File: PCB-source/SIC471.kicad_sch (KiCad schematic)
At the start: 15 parts, among them U9 SIC477ED-T1-GE3

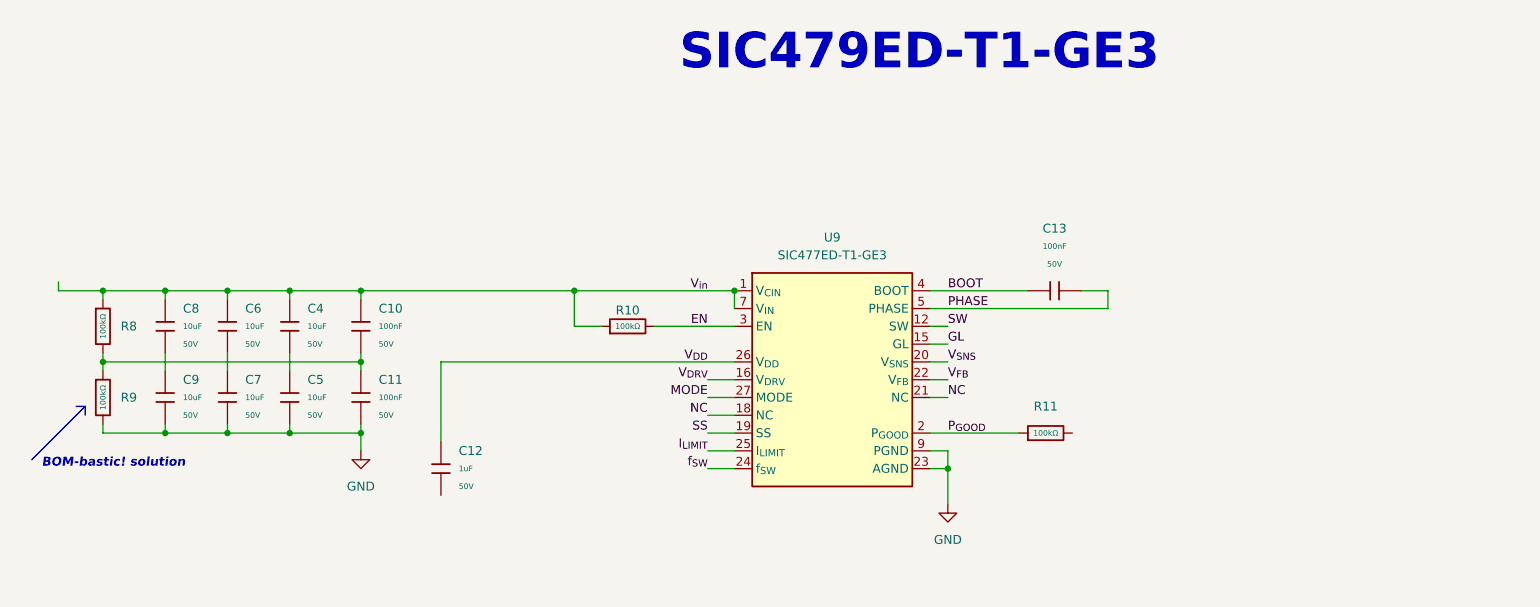
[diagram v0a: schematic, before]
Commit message: Finish component and diffpair placement
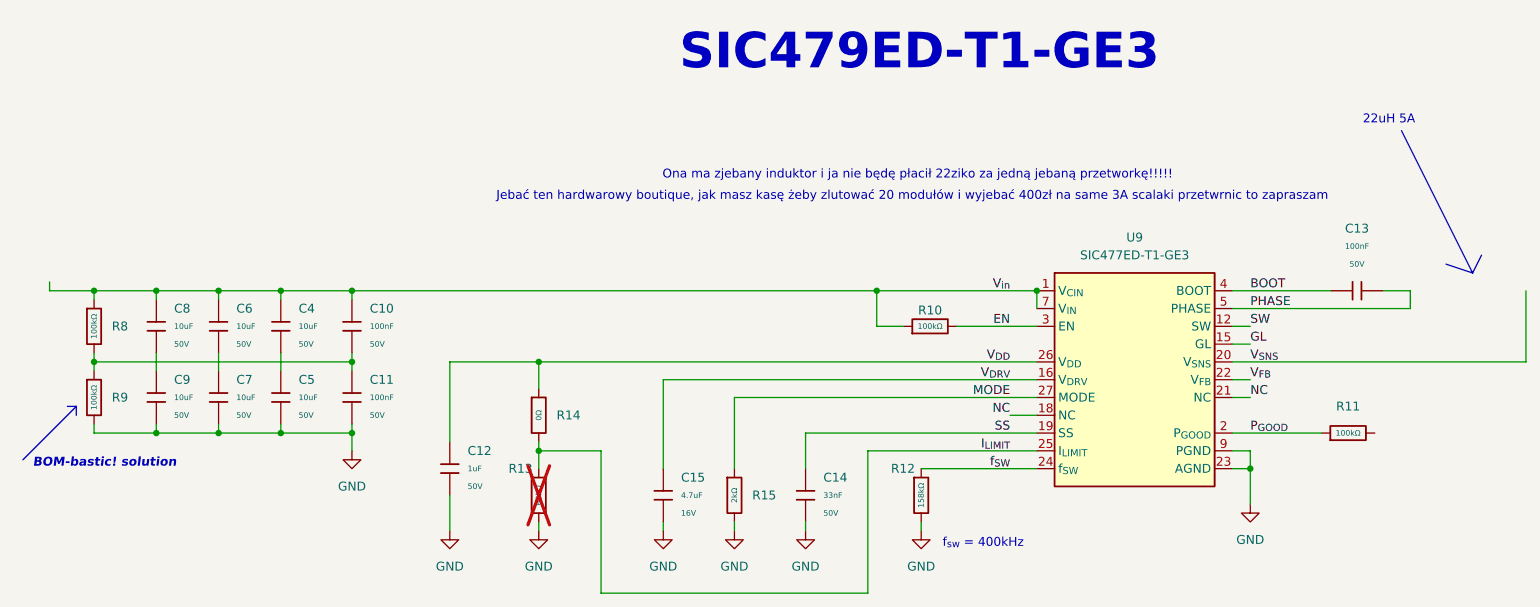
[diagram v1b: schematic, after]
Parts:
- added C14: 33nF, PCM_JLCPCB:C_0603, symbol PCM_JLCPCB-Capacitors:0603,33nF
- added C15: 4.7uF, PCM_JLCPCB:C_0603, symbol PCM_JLCPCB-Capacitors:0603,4.7uF
- added R12: 158kΩ, PCM_JLCPCB:R_0402, symbol PCM_JLCPCB-Resistors:0402,100kΩ
- added R13: 68kΩ, PCM_JLCPCB:R_0402, symbol PCM_JLCPCB-Resistors:0402,100kΩ
- added R14: 0Ω, PCM_JLCPCB:R_0402, symbol PCM_JLCPCB-Resistors:0402,0Ω
- added R15: 2kΩ, PCM_JLCPCB:R_0402, symbol PCM_JLCPCB-Resistors:0402,2kΩ
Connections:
- net GND: now also C12.2, C14.2, C15.2, R12.2, R13.2, R15.2
- net I_{LIMIT}: now also R13.1, R14.2
- net MODE: now also R15.1
- net SS: now also C14.1
- net V_{DD}: now also R14.1
- net V_{DRV}: now also C15.1
- net f_{SW}: now also R12.1
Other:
- note added: "22uH 5A"
- note added: "Jebać ten hardwarowy boutique, jak masz kasę żeby zlutować 20 modułów i wyjebać 400zł na same 3A scalaki przetwrnic to zapraszam"
- note added: "Ona ma zjebany induktor i ja nie będę płacił 22ziko za jedną jebaną przetworkę!!!!!"
- note added: "f_{sw} = 400kHz"
- moved on the sheet: C10, C11, C12, C13, C4, C5, C6, C7, C8, C9, R10, R11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
